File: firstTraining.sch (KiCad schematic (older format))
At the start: 8 parts, among them T1 Transformer_1P_SS, U1 L7805, U2 L78L33_SO8

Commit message: フットプリント設定, トランスはフットプリント要作成
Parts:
- C1, C2: footprint (none) -> Capacitor_THT:CP_Radial_D10.0mm_P5.00mm
- C3, C4: footprint (none) -> Capacitor_THT:C_Disc_D3.0mm_W1.6mm_P2.50mm
- D1, T1: footprint (none) -> Diode_THT:Diode_Bridge_DIP-4_W7.62mm_P5.08mm
- U1: footprint (none) -> Connector:FanPinHeader_1x03_P2.54mm_Vertical
- U2: footprint Package_SO:SOIC-8_3.9x4.9mm_P1.27mm -> Connector:FanPinHeader_1x03_P2.54mm_Vertical
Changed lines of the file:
@@
 F 0 "T1" H 3200 1878 50  0000 C CNN
 F 1 "Transformer_1P_SS" H 3200 1787 50  0000 C CNN
-F 2 "" H 3200 1500 50  0001 C CNN
+F 2 "Diode_THT:Diode_Bridge_DIP-4_W7.62mm_P5.08mm" H 3200 1500 50  0001 C CNN
 F 3 "~" H 3200 1500 50  0001 C CNN
 	1    3200 1500
@@
 F 0 "D1" H 4641 1546 50  0000 L CNN
 F 1 "D_Bridge_+-AA" H 4641 1455 50  0000 L CNN
-F 2 "" H 4300 1500 50  0001 C CNN
+F 2 "Diode_THT:Diode_Bridge_DIP-4_W7.62mm_P5.08mm" H 4300 1500 50  0001 C CNN
 F 3 "~" H 4300 1500 50  0001 C CNN
 	1    4300 1500
@@
 F 0 "C1" H 5715 1696 50  0000 L CNN
 F 1 "CP1" H 5715 1605 50  0000 L CNN
-F 2 "" H 5600 1650 50  0001 C CNN
+F 2 "Capacitor_THT:CP_Radial_D10.0mm_P5.00mm" H 5600 1650 50  0001 C CNN
 F 3 "~" H 5600 1650 50  0001 C CNN
 	1    5600 1650
@@
 F 0 "C2" H 5485 2154 50  0000 R CNN
 F 1 "CP1" H 5485 2245 50  0000 R CNN
-F 2 "" H 5600 2200 50  0001 C CNN
+F 2 "Capacitor_THT:CP_Radial_D10.0mm_P5.00mm" H 5600 2200 50  0001 C CNN
 F 3 "~" H 5600 2200 50  0001 C CNN
 	1    5600 2200
@@
 F 0 "C4" H 7315 2546 50  0000 L CNN
 F 1 "C" H 7315 2455 50  0000 L CNN
-F 2 "" H 7238 2350 50  0001 C CNN
+F 2 "Capacitor_THT:C_Disc_D3.0mm_W1.6mm_P2.50mm" H 7238 2350 50  0001 C CNN
 F 3 "~" H 7200 2500 50  0001 C CNN
 	1    7200 2500
@@
 F 0 "C3" H 7315 1696 50  0000 L CNN
 F 1 "C" H 7315 1605 50  0000 L CNN
-F 2 "" H 7238 1500 50  0001 C CNN
+F 2 "Capacitor_THT:C_Disc_D3.0mm_W1.6mm_P2.50mm" H 7238 1500 50  0001 C CNN
 F 3 "~" H 7200 1650 50  0001 C CNN
 	1    7200 1650
@@
 F 0 "U1" H 6500 1742 50  0000 C CNN
 F 1 "L7805" H 6500 1651 50  0000 C CNN
-F 2 "" H 6525 1350 50  0001 L CIN
+F 2 "Connector:FanPinHeader_1x03_P2.54mm_Vertical" H 6525 1350 50  0001 L CIN
 F 3 "http://www.st.com/content/ccc/resource/technical/document/datasheet/41/4f/b3/b0/12/d4/47/88/CD00000444.pdf/files/CD00000444.pdf/jcr:content/translations/en.CD00000444.pdf" H 6500 1450 50  0001 C CNN
 	1    6500 1500
@@
 F 0 "U2" H 6500 2592 50  0000 C CNN
 F 1 "L78L33_SO8" H 6500 2501 50  0000 C CNN
-F 2 "Package_SO:SOIC-8_3.9x4.9mm_P1.27mm" H 6600 2550 50  0001 C CIN
+F 2 "Connector:FanPinHeader_1x03_P2.54mm_Vertical" H 6600 2550 50  0001 C CIN
 F 3 "http://www.st.com/content/ccc/resource/technical/document/datasheet/15/55/e5/aa/23/5b/43/fd/CD00000446.pdf/files/CD00000446.pdf/jcr:content/translations/en.CD00000446.pdf" H 6700 2350 50  0001 C CNN
 	1    6500 2350

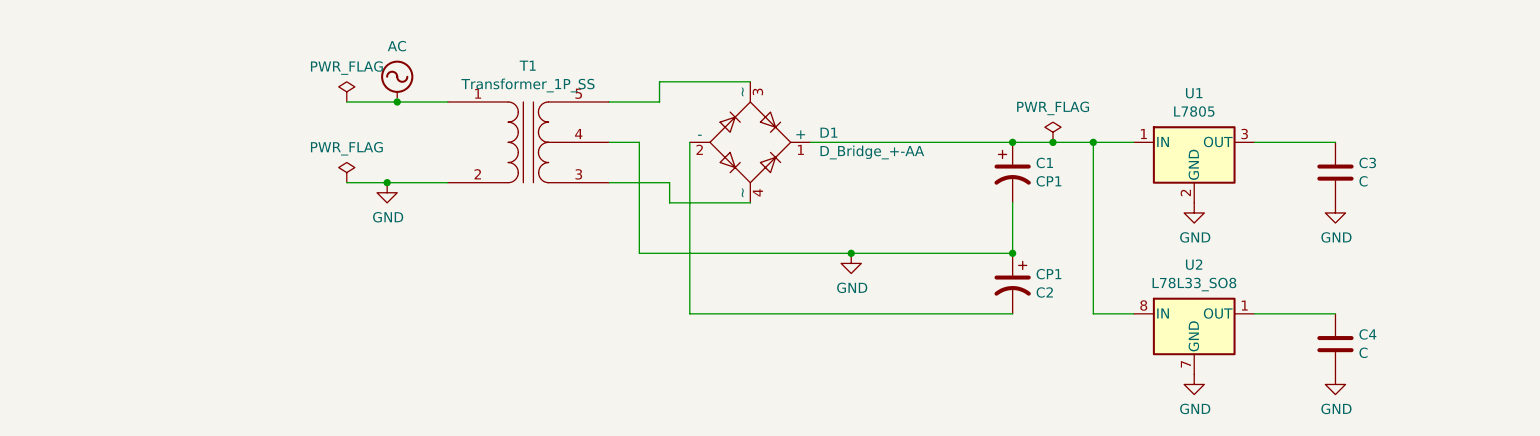
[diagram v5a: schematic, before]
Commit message: センタータップ式に修正
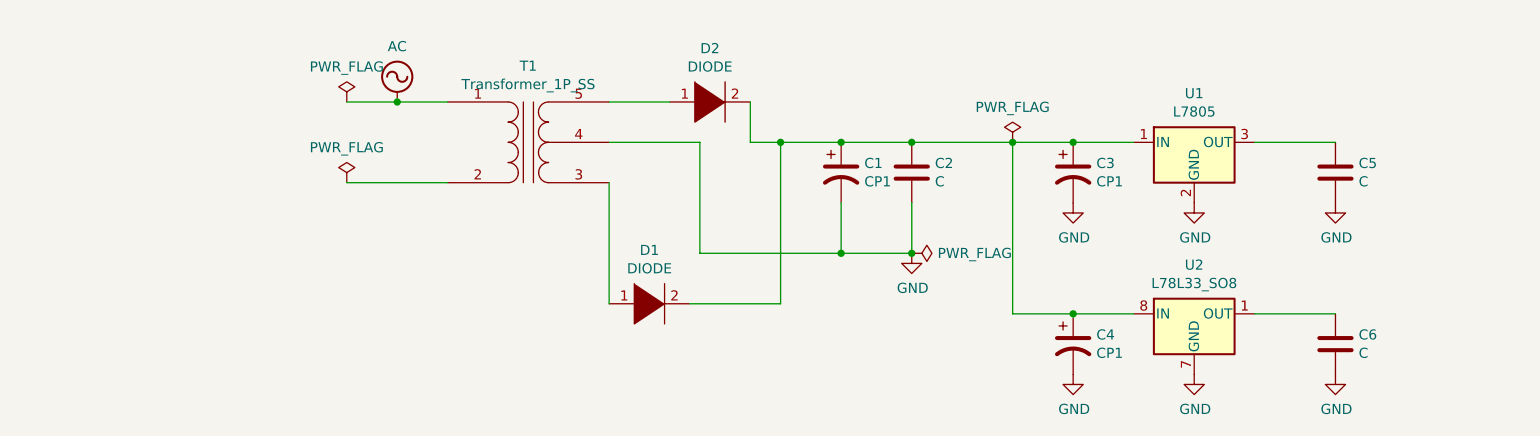
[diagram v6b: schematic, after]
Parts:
- removed C2: CP1, Capacitor_THT:CP_Radial_D10.0mm_P5.00mm, symbol Device:CP1
- removed D1: D_Bridge_+-AA, Diode_THT:Diode_Bridge_DIP-4_W7.62mm_P5.08mm, symbol Device:D_Bridge_+-AA
- added C2: C, symbol Device:C
- added C3, C4: CP1, symbol Device:CP1
- added D1, D2: DIODE, symbol pspice:DIODE
- renumbered C3 to C5, C4 to C6
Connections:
- net GND: now also C2.2, C3.2, C4.2; no longer T1.2 (AB)
- net at T1.3 (SA): now also D1.1 (K)
- net at T1.5 (SB): now also D2.1 (K)
- net at C1.1, U1.1 (IN), U2.8 (IN): now also C2.1, C3.1, C4.1, D1.2 (A), D2.2 (A)
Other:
- moved on the sheet: C1

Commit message: フットプリント再実施
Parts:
- C2, C3, C4: footprint (none) -> Capacitor_THT:CP_Radial_D10.0mm_P5.00mm
- D1, D2: footprint (none) -> Diode_THT:D_A-405_P7.62mm_Horizontal
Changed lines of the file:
@@
 F 0 "D1" H 3800 2565 50  0000 C CNN
 F 1 "DIODE" H 3800 2474 50  0000 C CNN
-F 2 "" H 3800 2300 50  0001 C CNN
+F 2 "Diode_THT:D_A-405_P7.62mm_Horizontal" H 3800 2300 50  0001 C CNN
 F 3 "~" H 3800 2300 50  0001 C CNN
 	1    3800 2300
@@
 F 0 "D2" H 4100 1565 50  0000 C CNN
 F 1 "DIODE" H 4100 1474 50  0000 C CNN
-F 2 "" H 4100 1300 50  0001 C CNN
+F 2 "Diode_THT:D_A-405_P7.62mm_Horizontal" H 4100 1300 50  0001 C CNN
 F 3 "~" H 4100 1300 50  0001 C CNN
 	1    4100 1300
@@
 F 0 "C2" H 5215 1696 50  0000 L CNN
 F 1 "C" H 5215 1605 50  0000 L CNN
-F 2 "" H 5138 1500 50  0001 C CNN
+F 2 "Capacitor_THT:CP_Radial_D10.0mm_P5.00mm" H 5138 1500 50  0001 C CNN
 F 3 "~" H 5100 1650 50  0001 C CNN
 	1    5100 1650
@@
 F 0 "C3" H 6015 1696 50  0000 L CNN
 F 1 "CP1" H 6015 1605 50  0000 L CNN
-F 2 "" H 5900 1650 50  0001 C CNN
+F 2 "Capacitor_THT:CP_Radial_D10.0mm_P5.00mm" H 5900 1650 50  0001 C CNN
 F 3 "~" H 5900 1650 50  0001 C CNN
 	1    5900 1650
@@
 F 0 "C4" H 6015 2546 50  0000 L CNN
 F 1 "CP1" H 6015 2455 50  0000 L CNN
-F 2 "" H 5900 2500 50  0001 C CNN
+F 2 "Capacitor_THT:CP_Radial_D10.0mm_P5.00mm" H 5900 2500 50  0001 C CNN
 F 3 "~" H 5900 2500 50  0001 C CNN
 	1    5900 2500
@@
 	2300 1700 2800 1700
 $Comp
-L power:GND #PWR?
+L power:GND #PWR0101
 U 1 1 5BD927B3
 P 5900 1800
-F 0 "#PWR?" H 5900 1550 50  0001 C CNN
+F 0 "#PWR0101" H 5900 1550 50  0001 C CNN
 F 1 "GND" H 5905 1627 50  0000 C CNN
 F 2 "" H 5900 1800 50  0001 C CNN
@@
 $EndComp
 $Comp
-L power:GND #PWR?
+L power:GND #PWR0102
 U 1 1 5BD927FD
 P 6500 1800
-F 0 "#PWR?" H 6500 1550 50  0001 C CNN
+F 0 "#PWR0102" H 6500 1550 50  0001 C CNN
 F 1 "GND" H 6505 1627 50  0000 C CNN
 F 2 "" H 6500 1800 50  0001 C CNN
@@
 $EndComp
 $Comp
-L power:GND #PWR?
+L power:GND #PWR0103
 U 1 1 5BD92847
 P 7200 1800
-F 0 "#PWR?" H 7200 1550 50  0001 C CNN
+F 0 "#PWR0103" H 7200 1550 50  0001 C CNN
 F 1 "GND" H 7205 1627 50  0000 C CNN
 F 2 "" H 7200 1800 50  0001 C CNN
@@
 $EndComp
 $Comp
-L power:GND #PWR?
+L power:GND #PWR0104
 U 1 1 5BD92891
 P 7200 2650
-F 0 "#PWR?" H 7200 2400 50  0001 C CNN
+F 0 "#PWR0104" H 7200 2400 50  0001 C CNN
 F 1 "GND" H 7205 2477 50  0000 C CNN
 F 2 "" H 7200 2650 50  0001 C CNN
@@
 $EndComp
 $Comp
-L power:GND #PWR?
+L power:GND #PWR0105
 U 1 1 5BD928DB
 P 6500 2650
-F 0 "#PWR?" H 6500 2400 50  0001 C CNN
+F 0 "#PWR0105" H 6500 2400 50  0001 C CNN
 F 1 "GND" H 6505 2477 50  0000 C CNN
 F 2 "" H 6500 2650 50  0001 C CNN
@@
 $EndComp
 $Comp
-L power:GND #PWR?
+L power:GND #PWR0106
 U 1 1 5BD92925
 P 5900 2650
-F 0 "#PWR?" H 5900 2400 50  0001 C CNN
+F 0 "#PWR0106" H 5900 2400 50  0001 C CNN
 F 1 "GND" H 5905 2477 50  0000 C CNN
 F 2 "" H 5900 2650 50  0001 C CNN
@@
 $EndComp
 $Comp
-L power:GND #PWR?
+L power:GND #PWR0107
 U 1 1 5BD9296F
 P 5100 2050
-F 0 "#PWR?" H 5100 1800 50  0001 C CNN
+F 0 "#PWR0107" H 5100 1800 50  0001 C CNN
 F 1 "GND" H 5105 1877 50  0000 C CNN
 F 2 "" H 5100 2050 50  0001 C CNN
@@
 Connection ~ 5100 2050
 $Comp
-L power:PWR_FLAG #FLG?
+L power:PWR_FLAG #FLG0102
 U 1 1 5BD929C0
 P 5100 2050
-F 0 "#FLG?" H 5100 2125 50  0001 C CNN
+F 0 "#FLG0102" H 5100 2125 50  0001 C CNN
 F 1 "PWR_FLAG" V 5100 2178 50  0000 L CNN
 F 2 "" H 5100 2050 50  0001 C CNN

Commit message: schが保存されていなかった
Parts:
- T1: footprint Diode_THT:Diode_Bridge_DIP-4_W7.62mm_P5.08mm -> newLib:HP-098
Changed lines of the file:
@@
 F 0 "T1" H 3200 1878 50  0000 C CNN
 F 1 "Transformer_1P_SS" H 3200 1787 50  0000 C CNN
-F 2 "Diode_THT:Diode_Bridge_DIP-4_W7.62mm_P5.08mm" H 3200 1500 50  0001 C CNN
+F 2 "newLib:HP-098" H 3200 1500 50  0001 C CNN
 F 3 "~" H 3200 1500 50  0001 C CNN
 	1    3200 1500
